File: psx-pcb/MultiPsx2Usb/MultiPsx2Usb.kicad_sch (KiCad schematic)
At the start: 23 parts, among them J1 AVR-UPDI-6, J2 USB_C_Receptacle_USB2.0_14P, SW1 SW_Push

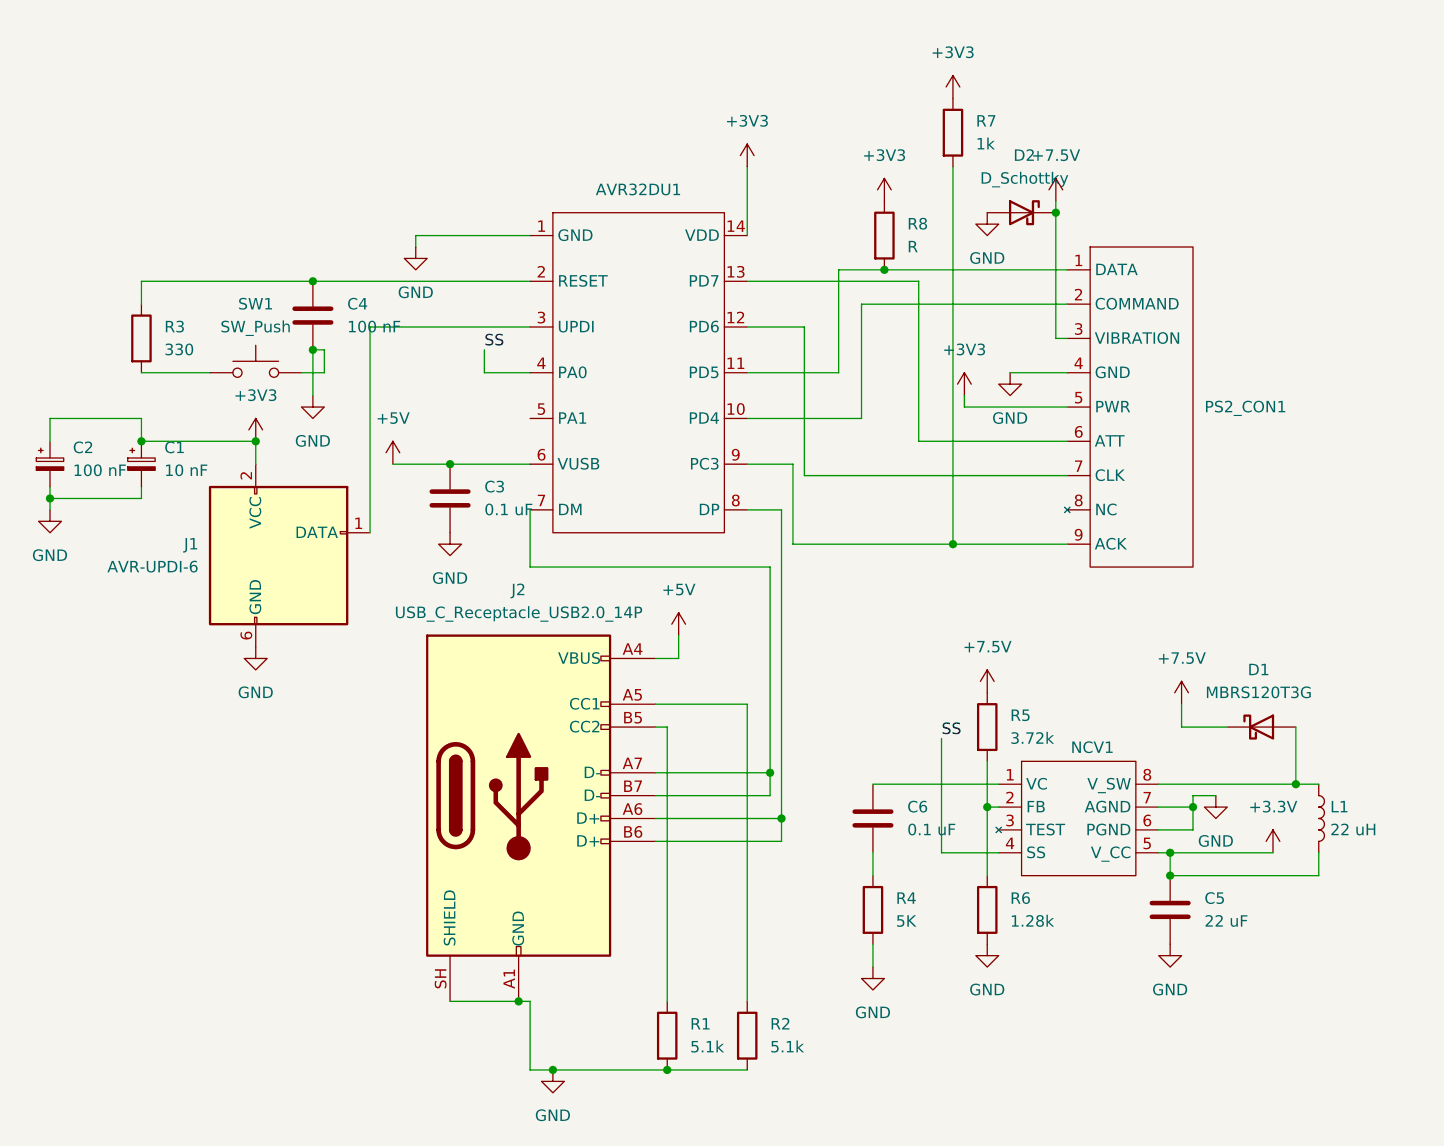
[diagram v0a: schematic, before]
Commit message: Populated PCB, finished adding everything I should need
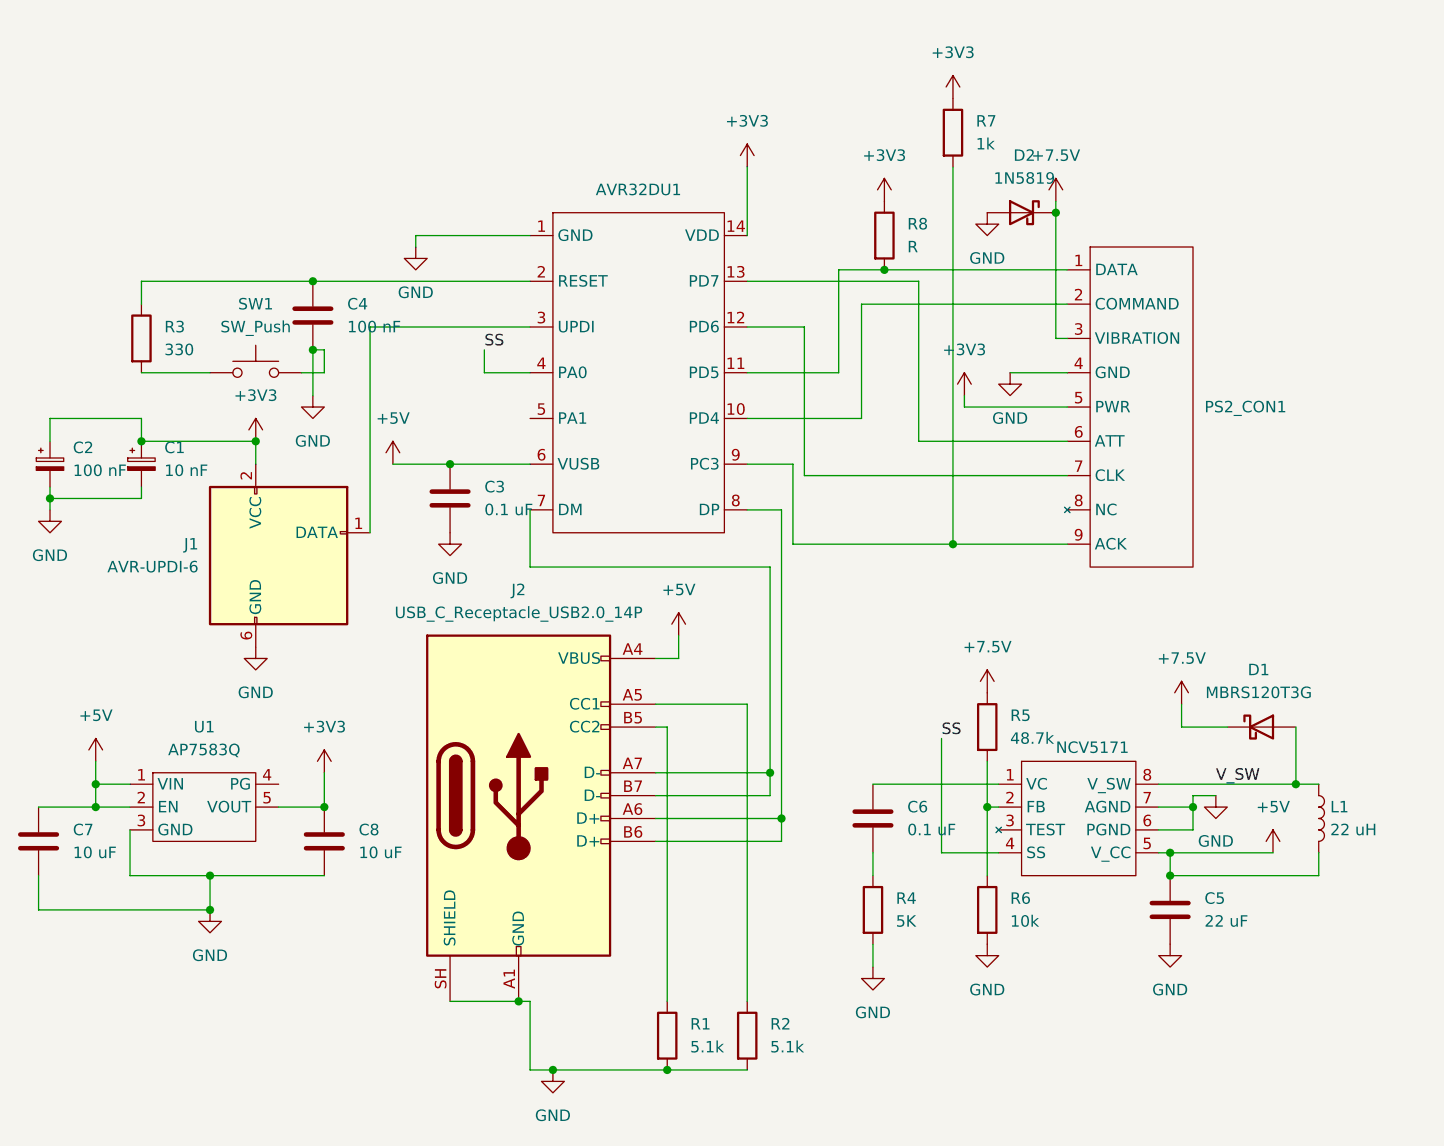
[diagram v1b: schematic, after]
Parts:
- added C7, C8: 10 uF, Capacitor_SMD:C_0603_1608Metric_Pad1.08x0.95mm_HandSolder, symbol Device:C
- added U1: AP7583Q, Package_TO_SOT_SMD:TO-252-5_TabPin3, symbol avr32du:AP7583Q
- D2: value D_Schottky -> 1N5819; footprint (none) -> Diode_SMD:D_SOD-123
- J1: footprint (none) -> Connector_PinHeader_2.54mm:PinHeader_2x03_P2.54mm_Vertical
- J2: footprint (none) -> Connector_USB:USB_C_Receptacle_GCT_USB4105-xx-A_16P_TopMnt_Horizontal
- R5: value 3.72k -> 48.7k
- R6: value 1.28k -> 10k
- renumbered NCV1 to NCV5171
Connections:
- net +3.3V is gone; now on net +5V: C5.1, L1.2, NCV5171.5 (V_CC)
- net +3V3: now also C8.1, U1.5 (VOUT)
- net +5V: now also C7.1, U1.1 (VIN), U1.2 (EN)
- net GND: now also C7.2, C8.2, U1.3 (GND)
- net V_SW: now reaches D1.2 (A), L1.1, NCV5171.8 (V_SW)

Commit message: GND track width increased to 20 mils to match +7.5V, still need to update PCB
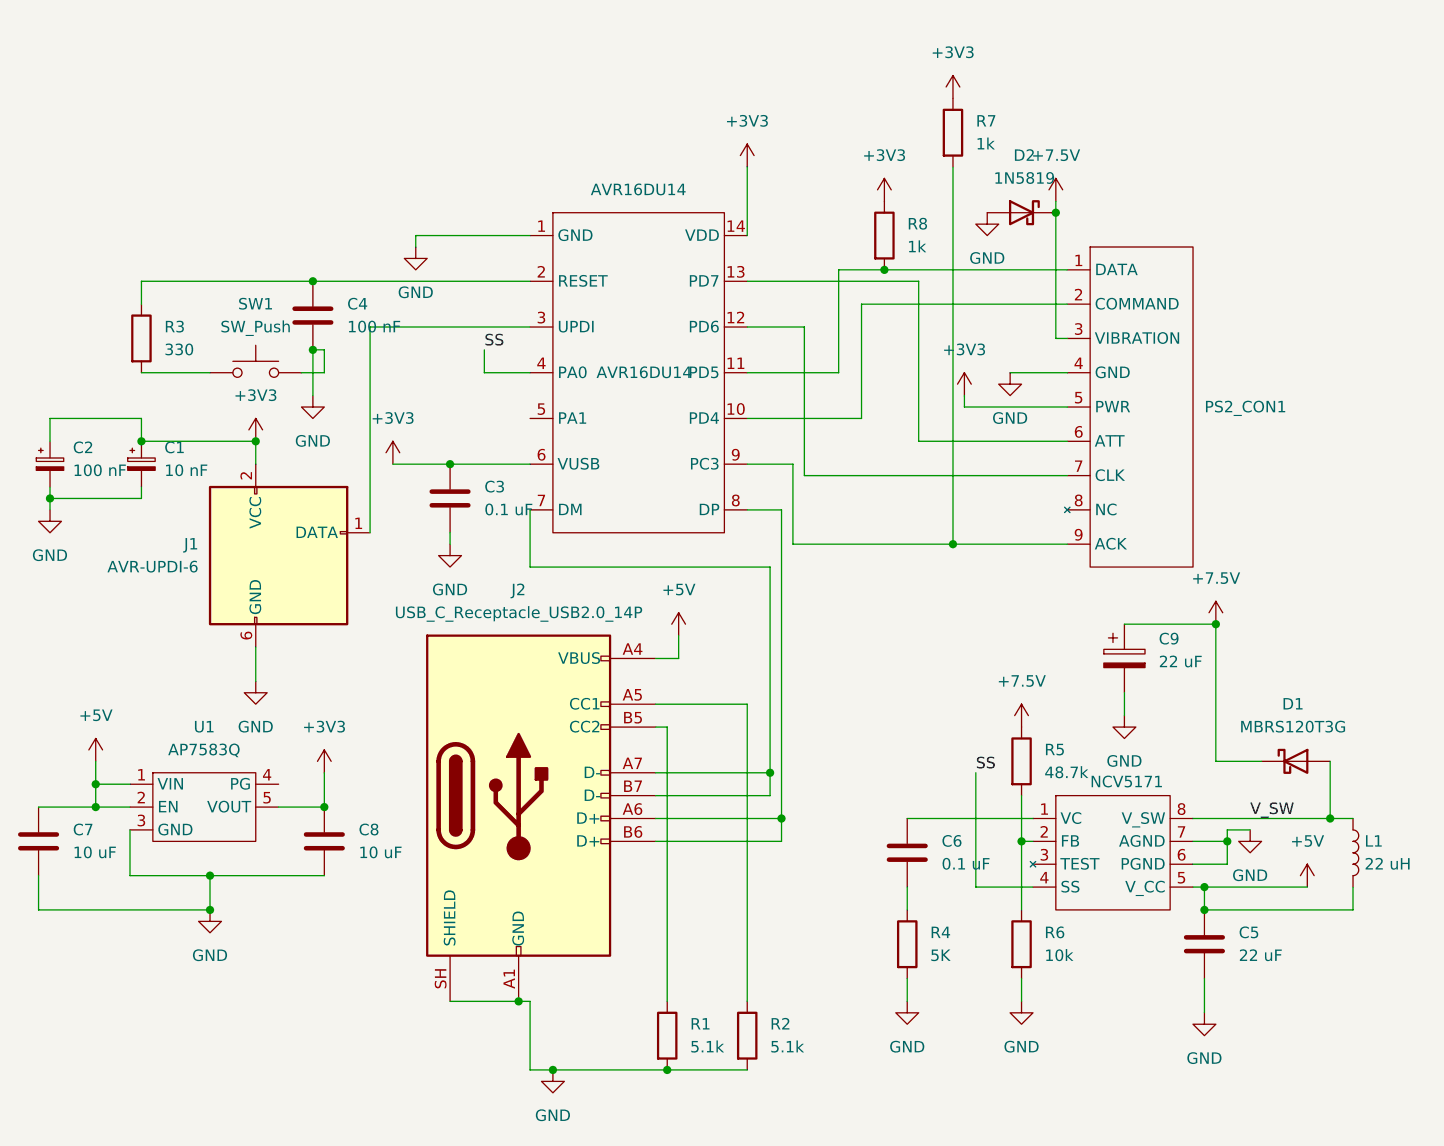
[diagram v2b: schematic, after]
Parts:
- added C9: 22 uF, symbol Device:C_Polarized
- AVR16DU14: renamed from AVR32DU1; value (none) -> AVR16DU14
- R8: value R -> 1k
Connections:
- net +3V3: now also AVR16DU14.6 (VUSB), C3.1
- net +5V: no longer AVR16DU14.6 (VUSB), C3.1
- net +7.5V: now also C9.1
- net GND: now also C9.2
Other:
- moved on the sheet: C5, C6, D1, L1, NCV5171, R4, R5, R6

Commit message: fixed inductor footprint. added 6-pin FTDI header. connected V_USB to 3.3V instead of 5V.
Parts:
- removed C9: 22 uF, symbol Device:C_Polarized
- added C9: 22 uF, Capacitor_SMD:C_0603_1608Metric_Pad1.08x0.95mm_HandSolder, symbol Device:C
- added J3: UART, Connector_PinHeader_2.54mm:PinHeader_1x06_P2.54mm_Vertical, symbol Connector_Generic:Conn_01x06
- L1: footprint Inductor_SMD:L_0603_1608Metric_Pad1.05x0.95mm_HandSolder -> Inductor_SMD:L_Bourns_SRN6045TA
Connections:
- net +3V3: now also J3.3 (Pin_3)
- net +7.5V: now also C9.1
- net GND: now also C9.2, J3.1 (Pin_1)
- net SS: no longer names the net of NCV5171.4 (SS)
- net SS: no longer AVR16DU14.4 (PA0)
- new net TxD: AVR16DU14.4 (PA0), J3.4 (Pin_4)

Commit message: Added circuitry to allow for serial TX, which is switchable with a microswitch to USB CC pin voltage measurement. Added player 2 ATT pin support
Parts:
- added D3: BAT54C, Package_TO_SOT_SMD:SOT-23, symbol Diode:BAT54C
- added J4: (no value), avr32du:PS2_P2, symbol avr32du:PS2_P2
- added SW2: SW_Nidec_CAS-120A1, Button_Switch_SMD:Nidec_Copal_CAS-120A, symbol Switch:SW_Nidec_CAS-120A1
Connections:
- net TxD: now also SW2.3 (A); no longer AVR16DU14.4 (PA0)
- net at J2.A5 (CC1), R2.1: now also D3.2
- net at J2.B5 (CC2), R1.1: now also D3.1
- net P2_ATT: now reaches AVR16DU14.5 (PA1)
- net P2_ATT: now also J4.1 (P2_ATT)
- new net: AVR16DU14.4 (PA0), SW2.2 (B)
- new net USB_CC: D3.3, SW2.1 (C)
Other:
- moved on the sheet: R2
